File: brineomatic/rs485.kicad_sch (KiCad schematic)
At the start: 12 parts, among them J22 3.5mm, J23 3.5mm, U10 MAX3485

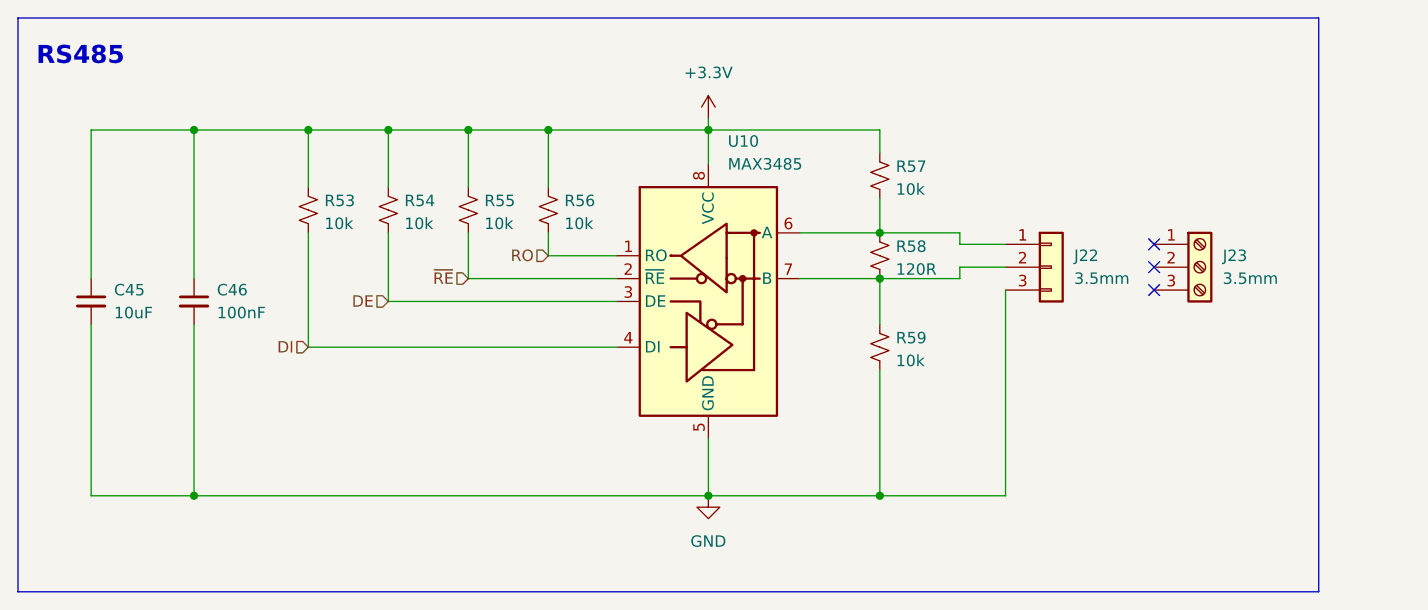
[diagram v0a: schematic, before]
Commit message: stacked tds, removed stepper vref, pulled in esp32-s3 schematic, added extra relay output
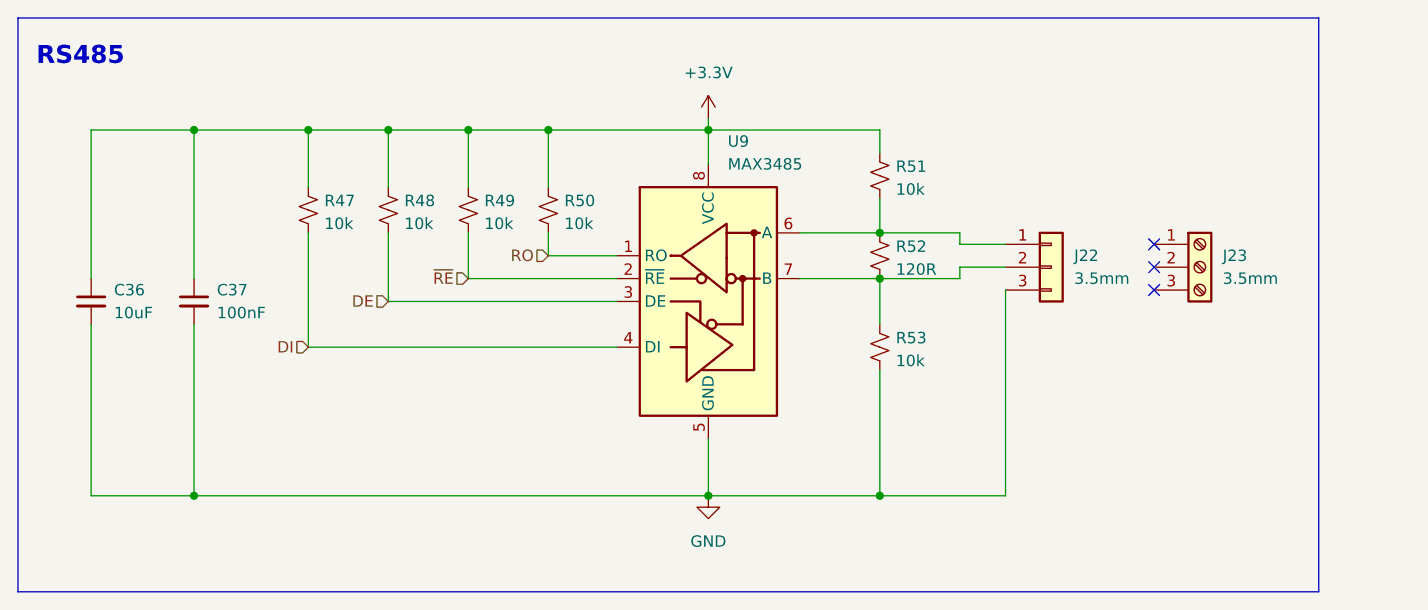
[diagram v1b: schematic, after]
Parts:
- renumbered C45 to C36, C46 to C37, R53 to R47, R54 to R48, R55 to R49, R56 to R50, R57 to R51, R58 to R52, R59 to R53, U10 to U9
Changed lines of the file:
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@@
 		(dnp no)
 		(fields_autoplaced yes)
-		(property "Reference" "#PWR050"
+		(property "Reference" "#PWR066"
 			(at 140.97 129.54 0)
 			(effects
@@
 			(project "brineomatic"
 				(path "/96477ae2-ef08-48f3-8dd4-fe4478541f68/ecabf60a-7f79-4ba0-9fc6-a1e702c2d5f0"
-					(reference "#PWR050")
+					(reference "#PWR066")
 					(unit 1)
 				)
@@
 		(on_board yes)
 		(dnp no)
-		(property "Reference" "R59"
+		(property "Reference" "R53"
 			(at 161.798 105.664 0)
 			(effects
@@
 			(project "brineomatic"
 				(path "/96477ae2-ef08-48f3-8dd4-fe4478541f68/ecabf60a-7f79-4ba0-9fc6-a1e702c2d5f0"
-					(reference "R59")
+					(reference "R53")
 					(unit 1)
 				)
@@
 		(on_board yes)
 		(dnp no)
-		(property "Reference" "R53"
+		(property "Reference" "R47"
 			(at 98.298 90.424 0)
 			(effects
@@
 			(project "brineomatic"
 				(path "/96477ae2-ef08-48f3-8dd4-fe4478541f68/ecabf60a-7f79-4ba0-9fc6-a1e702c2d5f0"
-					(reference "R53")
+					(reference "R47")
 					(unit 1)
 				)
@@
 		(on_board yes)
 		(dnp no)
-		(property "Reference" "C45"
+		(property "Reference" "C36"
 			(at 74.93 100.3363 0)
 			(effects
@@
 			(project "brineomatic"
 				(path "/96477ae2-ef08-48f3-8dd4-fe4478541f68/ecabf60a-7f79-4ba0-9fc6-a1e702c2d5f0"
-					(reference "C45")
+					(reference "C36")
 					(unit 1)
 				)
@@
 		(on_board yes)
 		(dnp no)
-		(property "Reference" "R55"
+		(property "Reference" "R49"
 			(at 116.078 90.424 0)
 			(effects
@@
 			(project "brineomatic"
 				(path "/96477ae2-ef08-48f3-8dd4-fe4478541f68/ecabf60a-7f79-4ba0-9fc6-a1e702c2d5f0"
-					(reference "R55")
+					(reference "R49")
 					(unit 1)
 				)
@@
 		(on_board yes)
 		(dnp no)
-		(property "Reference" "R56"
+		(property "Reference" "R50"
 			(at 124.968 90.424 0)
 			(effects
@@
 			(project "brineomatic"
 				(path "/96477ae2-ef08-48f3-8dd4-fe4478541f68/ecabf60a-7f79-4ba0-9fc6-a1e702c2d5f0"
-					(reference "R56")
+					(reference "R50")
 					(unit 1)
 				)
@@
 		(on_board yes)
 		(dnp no)
-		(property "Reference" "R58"
+		(property "Reference" "R52"
 			(at 161.798 95.504 0)
 			(effects
@@
 			(project "brineomatic"
 				(path "/96477ae2-ef08-48f3-8dd4-fe4478541f68/ecabf60a-7f79-4ba0-9fc6-a1e702c2d5f0"
-					(reference "R58")
+					(reference "R52")
 					(unit 1)
 				)
@@
 		(dnp no)
 		(fields_autoplaced yes)
-		(property "Reference" "C46"
+		(property "Reference" "C37"
 			(at 86.36 100.3363 0)
 			(effects
@@
 			(project "brineomatic"
 				(path "/96477ae2-ef08-48f3-8dd4-fe4478541f68/ecabf60a-7f79-4ba0-9fc6-a1e702c2d5f0"
-					(reference "C46")
+					(reference "C37")
 					(unit 1)
 				)
@@
 		(dnp no)
 		(fields_autoplaced yes)
-		(property "Reference" "U10"
+		(property "Reference" "U9"
 			(at 143.1133 83.82 0)
 			(effects
@@
 			(project ""
 				(path "/96477ae2-ef08-48f3-8dd4-fe4478541f68/ecabf60a-7f79-4ba0-9fc6-a1e702c2d5f0"
-					(reference "U10")
+					(reference "U9")
 					(unit 1)
 				)
@@
 		(dnp no)
 		(fields_autoplaced yes)
-		(property "Reference" "#PWR049"
+		(property "Reference" "#PWR065"
 			(at 140.97 85.09 0)
 			(effects
@@
 			(project ""
 				(path "/96477ae2-ef08-48f3-8dd4-fe4478541f68/ecabf60a-7f79-4ba0-9fc6-a1e702c2d5f0"
-					(reference "#PWR049")
+					(reference "#PWR065")
 					(unit 1)
 				)
@@
 		(on_board yes)
 		(dnp no)
-		(property "Reference" "R54"
+		(property "Reference" "R48"
 			(at 107.188 90.424 0)
 			(effects
@@
 			(project "brineomatic"
 				(path "/96477ae2-ef08-48f3-8dd4-fe4478541f68/ecabf60a-7f79-4ba0-9fc6-a1e702c2d5f0"
-					(reference "R54")
+					(reference "R48")
 					(unit 1)
 				)
@@
 		(on_board yes)
 		(dnp no)
-		(property "Reference" "R57"
+		(property "Reference" "R51"
 			(at 161.798 86.614 0)
 			(effects
@@
 			(project "brineomatic"
 				(path "/96477ae2-ef08-48f3-8dd4-fe4478541f68/ecabf60a-7f79-4ba0-9fc6-a1e702c2d5f0"
-					(reference "R57")
-					(unit 1)
-				)
+					(reference "R51")
+					(unit 1)
+				)

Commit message: added sendit piezo
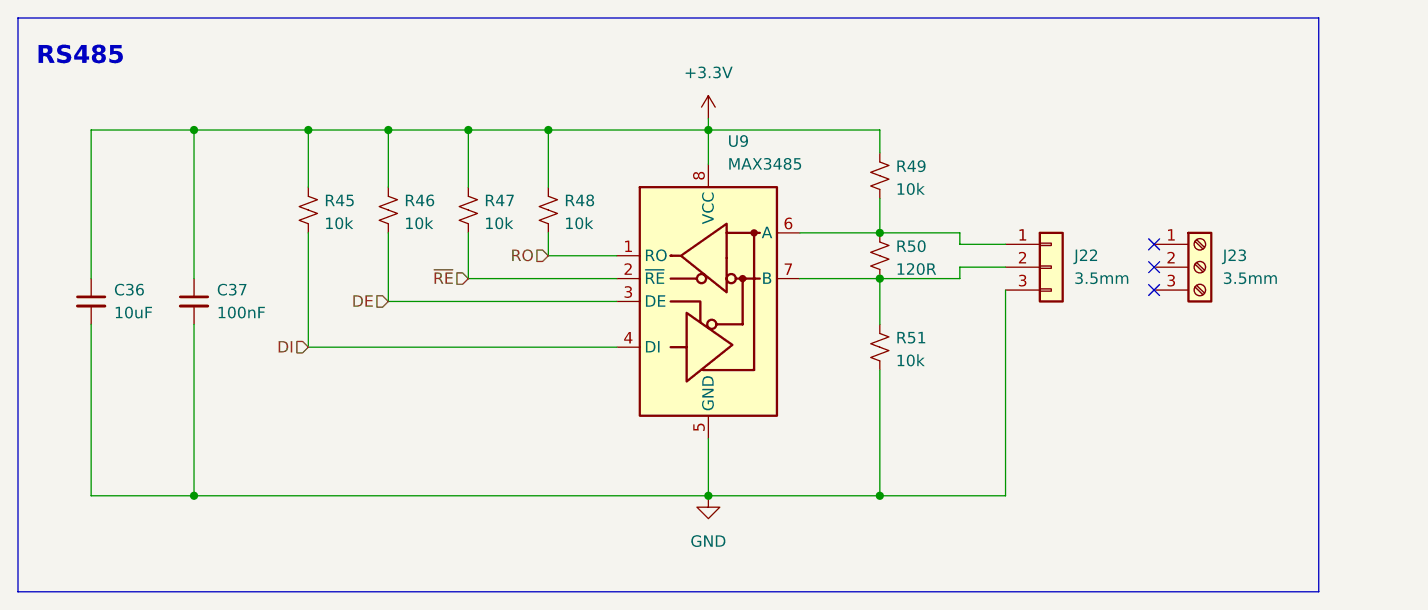
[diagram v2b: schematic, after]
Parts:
- renumbered R47 to R45, R48 to R46, R49 to R47, R50 to R48, R51 to R49, R52 to R50, R53 to R51
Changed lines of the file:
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@@
 		(on_board yes)
 		(dnp no)
-		(property "Reference" "R53"
+		(property "Reference" "R51"
 			(at 161.798 105.664 0)
 			(effects
@@
 			(project "brineomatic"
 				(path "/96477ae2-ef08-48f3-8dd4-fe4478541f68/ecabf60a-7f79-4ba0-9fc6-a1e702c2d5f0"
-					(reference "R53")
+					(reference "R51")
 					(unit 1)
 				)
@@
 		(on_board yes)
 		(dnp no)
-		(property "Reference" "R47"
+		(property "Reference" "R45"
 			(at 98.298 90.424 0)
 			(effects
@@
 			(project "brineomatic"
 				(path "/96477ae2-ef08-48f3-8dd4-fe4478541f68/ecabf60a-7f79-4ba0-9fc6-a1e702c2d5f0"
-					(reference "R47")
+					(reference "R45")
 					(unit 1)
 				)
@@
 		(on_board yes)
 		(dnp no)
-		(property "Reference" "R49"
+		(property "Reference" "R47"
 			(at 116.078 90.424 0)
 			(effects
@@
 			(project "brineomatic"
 				(path "/96477ae2-ef08-48f3-8dd4-fe4478541f68/ecabf60a-7f79-4ba0-9fc6-a1e702c2d5f0"
-					(reference "R49")
+					(reference "R47")
 					(unit 1)
 				)
@@
 		(on_board yes)
 		(dnp no)
-		(property "Reference" "R50"
+		(property "Reference" "R48"
 			(at 124.968 90.424 0)
 			(effects
@@
 			(project "brineomatic"
 				(path "/96477ae2-ef08-48f3-8dd4-fe4478541f68/ecabf60a-7f79-4ba0-9fc6-a1e702c2d5f0"
-					(reference "R50")
+					(reference "R48")
 					(unit 1)
 				)
@@
 		(on_board yes)
 		(dnp no)
-		(property "Reference" "R52"
+		(property "Reference" "R50"
 			(at 161.798 95.504 0)
 			(effects
@@
 			(project "brineomatic"
 				(path "/96477ae2-ef08-48f3-8dd4-fe4478541f68/ecabf60a-7f79-4ba0-9fc6-a1e702c2d5f0"
-					(reference "R52")
+					(reference "R50")
 					(unit 1)
 				)
@@
 		(on_board yes)
 		(dnp no)
-		(property "Reference" "R48"
+		(property "Reference" "R46"
 			(at 107.188 90.424 0)
 			(effects
@@
 			(project "brineomatic"
 				(path "/96477ae2-ef08-48f3-8dd4-fe4478541f68/ecabf60a-7f79-4ba0-9fc6-a1e702c2d5f0"
-					(reference "R48")
+					(reference "R46")
 					(unit 1)
 				)
@@
 		(on_board yes)
 		(dnp no)
-		(property "Reference" "R51"
+		(property "Reference" "R49"
 			(at 161.798 86.614 0)
 			(effects
@@
 			(project "brineomatic"
 				(path "/96477ae2-ef08-48f3-8dd4-fe4478541f68/ecabf60a-7f79-4ba0-9fc6-a1e702c2d5f0"
-					(reference "R51")
-					(unit 1)
-				)
+					(reference "R49")
+					(unit 1)
+				)

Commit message: all connectors are now flush withe 3mm outside edge of the case
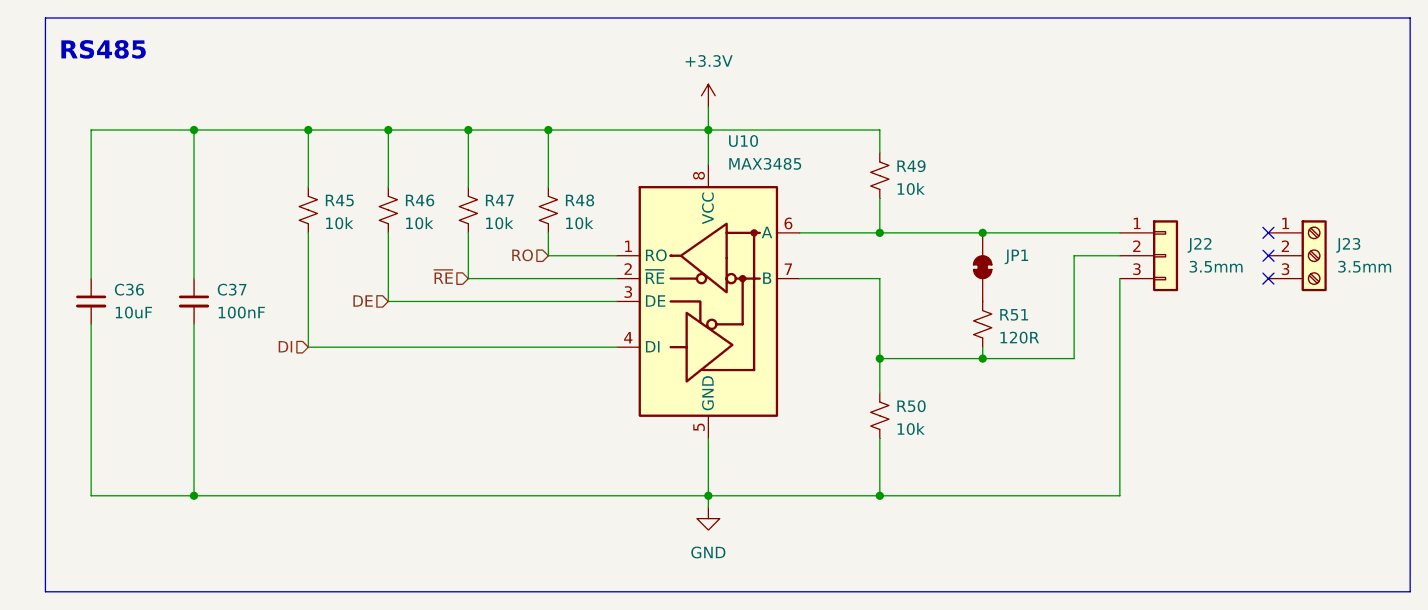
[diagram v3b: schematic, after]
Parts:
- added JP1: SolderJumper_2_Bridged, Jumper:SolderJumper-2_P1.3mm_Bridged_RoundedPad1.0x1.5mm, symbol Jumper:SolderJumper_2_Bridged
- renumbered R51 to R50, R50 to R51, U9 to U10
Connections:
- net at J22.1 (Pin_1), R49.1, U10.6 (A): now also JP1.2 (B); no longer R51.2
- new net: JP1.1 (A), R51.2
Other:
- moved on the sheet: J22, J23, R50, R51

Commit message: schematic tidy, usb c position verified, component placement work.
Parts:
- R50: renamed from R49; value 10k -> 20k
- R51: renamed from R50; value 10k -> 20k
- renumbered R45 to R46, R46 to R47, R47 to R48, R48 to R49, R51 to R52
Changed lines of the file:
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@@
 		(dnp no)
 		(fields_autoplaced yes)
-		(property "Reference" "#PWR066"
+		(property "Reference" "#PWR068"
 			(at 140.97 130.81 0)
 			(effects
@@
 			(project "brineomatic"
 				(path "/96477ae2-ef08-48f3-8dd4-fe4478541f68/ecabf60a-7f79-4ba0-9fc6-a1e702c2d5f0"
-					(reference "#PWR066")
+					(reference "#PWR068")
 					(unit 1)
 				)
@@
 		(on_board yes)
 		(dnp no)
-		(property "Reference" "R50"
+		(property "Reference" "R51"
 			(at 161.798 113.284 0)
 			(effects
@@
 			)
 		)
-		(property "Value" "10k"
+		(property "Value" "20k"
 			(at 161.798 115.824 0)
 			(effects
@@
 			(project "brineomatic"
 				(path "/96477ae2-ef08-48f3-8dd4-fe4478541f68/ecabf60a-7f79-4ba0-9fc6-a1e702c2d5f0"
-					(reference "R50")
+					(reference "R51")
 					(unit 1)
 				)
@@
 		(on_board yes)
 		(dnp no)
-		(property "Reference" "R45"
+		(property "Reference" "R46"
 			(at 98.298 90.424 0)
 			(effects
@@
 			(project "brineomatic"
 				(path "/96477ae2-ef08-48f3-8dd4-fe4478541f68/ecabf60a-7f79-4ba0-9fc6-a1e702c2d5f0"
-					(reference "R45")
+					(reference "R46")
 					(unit 1)
 				)
@@
 		(on_board yes)
 		(dnp no)
-		(property "Reference" "R47"
+		(property "Reference" "R48"
 			(at 116.078 90.424 0)
 			(effects
@@
 			(project "brineomatic"
 				(path "/96477ae2-ef08-48f3-8dd4-fe4478541f68/ecabf60a-7f79-4ba0-9fc6-a1e702c2d5f0"
-					(reference "R47")
+					(reference "R48")
 					(unit 1)
 				)
@@
 		(on_board yes)
 		(dnp no)
-		(property "Reference" "R48"
+		(property "Reference" "R49"
 			(at 124.968 90.424 0)
 			(effects
@@
 			(project "brineomatic"
 				(path "/96477ae2-ef08-48f3-8dd4-fe4478541f68/ecabf60a-7f79-4ba0-9fc6-a1e702c2d5f0"
-					(reference "R48")
+					(reference "R49")
 					(unit 1)
 				)
@@
 		(on_board yes)
 		(dnp no)
-		(property "Reference" "R51"
+		(property "Reference" "R52"
 			(at 173.228 103.124 0)
 			(effects
@@
 			(project "brineomatic"
 				(path "/96477ae2-ef08-48f3-8dd4-fe4478541f68/ecabf60a-7f79-4ba0-9fc6-a1e702c2d5f0"
-					(reference "R51")
+					(reference "R52")
 					(unit 1)
 				)
@@
 		(dnp no)
 		(fields_autoplaced yes)
-		(property "Reference" "#PWR065"
+		(property "Reference" "#PWR067"
 			(at 140.97 83.82 0)
 			(effects
@@
 			(project ""
 				(path "/96477ae2-ef08-48f3-8dd4-fe4478541f68/ecabf60a-7f79-4ba0-9fc6-a1e702c2d5f0"
-					(reference "#PWR065")
+					(reference "#PWR067")
 					(unit 1)
 				)
@@
 		(on_board yes)
 		(dnp no)
-		(property "Reference" "R46"
+		(property "Reference" "R47"
 			(at 107.188 90.424 0)
 			(effects
@@
 			(project "brineomatic"
 				(path "/96477ae2-ef08-48f3-8dd4-fe4478541f68/ecabf60a-7f79-4ba0-9fc6-a1e702c2d5f0"
-					(reference "R46")
+					(reference "R47")
 					(unit 1)
 				)
@@
 		(on_board yes)
 		(dnp no)
-		(property "Reference" "R49"
+		(property "Reference" "R50"
 			(at 161.798 86.614 0)
 			(effects
@@
 			)
 		)
-		(property "Value" "10k"
+		(property "Value" "20k"
 			(at 161.798 89.154 0)
 			(effects
@@
 			(project "brineomatic"
 				(path "/96477ae2-ef08-48f3-8dd4-fe4478541f68/ecabf60a-7f79-4ba0-9fc6-a1e702c2d5f0"
-					(reference "R49")
-					(unit 1)
-				)
+					(reference "R50")
+					(unit 1)
+				)

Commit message: added voltage divider to vref.  more component shuffling.
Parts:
- renumbered R46 to R48, R47 to R49, R48 to R50, R49 to R51, R50 to R52, R51 to R53, R52 to R54
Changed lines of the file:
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@@
 		(title "https://github.com/hoeken/brineomatic")
 		(date "2025-08-28")
-		(rev "B")
+		(rev "C")
 	)
 	(rectangle
@@
 		(on_board yes)
 		(dnp no)
-		(property "Reference" "R51"
+		(property "Reference" "R53"
 			(at 161.798 113.284 0)
 			(effects
@@
 			(project "brineomatic"
 				(path "/96477ae2-ef08-48f3-8dd4-fe4478541f68/ecabf60a-7f79-4ba0-9fc6-a1e702c2d5f0"
-					(reference "R51")
+					(reference "R53")
 					(unit 1)
 				)
@@
 		(on_board yes)
 		(dnp no)
-		(property "Reference" "R46"
+		(property "Reference" "R48"
 			(at 98.298 90.424 0)
 			(effects
@@
 			(project "brineomatic"
 				(path "/96477ae2-ef08-48f3-8dd4-fe4478541f68/ecabf60a-7f79-4ba0-9fc6-a1e702c2d5f0"
-					(reference "R46")
+					(reference "R48")
 					(unit 1)
 				)
@@
 		(on_board yes)
 		(dnp no)
-		(property "Reference" "R48"
+		(property "Reference" "R50"
 			(at 116.078 90.424 0)
 			(effects
@@
 			(project "brineomatic"
 				(path "/96477ae2-ef08-48f3-8dd4-fe4478541f68/ecabf60a-7f79-4ba0-9fc6-a1e702c2d5f0"
-					(reference "R48")
+					(reference "R50")
 					(unit 1)
 				)
@@
 		(on_board yes)
 		(dnp no)
-		(property "Reference" "R49"
+		(property "Reference" "R51"
 			(at 124.968 90.424 0)
 			(effects
@@
 			(project "brineomatic"
 				(path "/96477ae2-ef08-48f3-8dd4-fe4478541f68/ecabf60a-7f79-4ba0-9fc6-a1e702c2d5f0"
-					(reference "R49")
+					(reference "R51")
 					(unit 1)
 				)
@@
 		(on_board yes)
 		(dnp no)
-		(property "Reference" "R52"
+		(property "Reference" "R54"
 			(at 173.228 103.124 0)
 			(effects
@@
 			(project "brineomatic"
 				(path "/96477ae2-ef08-48f3-8dd4-fe4478541f68/ecabf60a-7f79-4ba0-9fc6-a1e702c2d5f0"
-					(reference "R52")
+					(reference "R54")
 					(unit 1)
 				)
@@
 		(on_board yes)
 		(dnp no)
-		(property "Reference" "R47"
+		(property "Reference" "R49"
 			(at 107.188 90.424 0)
 			(effects
@@
 			(project "brineomatic"
 				(path "/96477ae2-ef08-48f3-8dd4-fe4478541f68/ecabf60a-7f79-4ba0-9fc6-a1e702c2d5f0"
-					(reference "R47")
+					(reference "R49")
 					(unit 1)
 				)
@@
 		(on_board yes)
 		(dnp no)
-		(property "Reference" "R50"
+		(property "Reference" "R52"
 			(at 161.798 86.614 0)
 			(effects
@@
 			(project "brineomatic"
 				(path "/96477ae2-ef08-48f3-8dd4-fe4478541f68/ecabf60a-7f79-4ba0-9fc6-a1e702c2d5f0"
-					(reference "R50")
+					(reference "R52")
 					(unit 1)
 				)
